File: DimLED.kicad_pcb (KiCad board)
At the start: 2 copper layers, 116 x 26 mm, 15 parts, among them J1 Input Power Terminal, J2 DC005, J3 Conn_01x05, J4 Output LED Terminal, J5 Conn_01x03, SW1 IO BTN, SW2 RST BTN, U1 MP1584 Module, U2 ESP-01, U3 XY-MOS Module

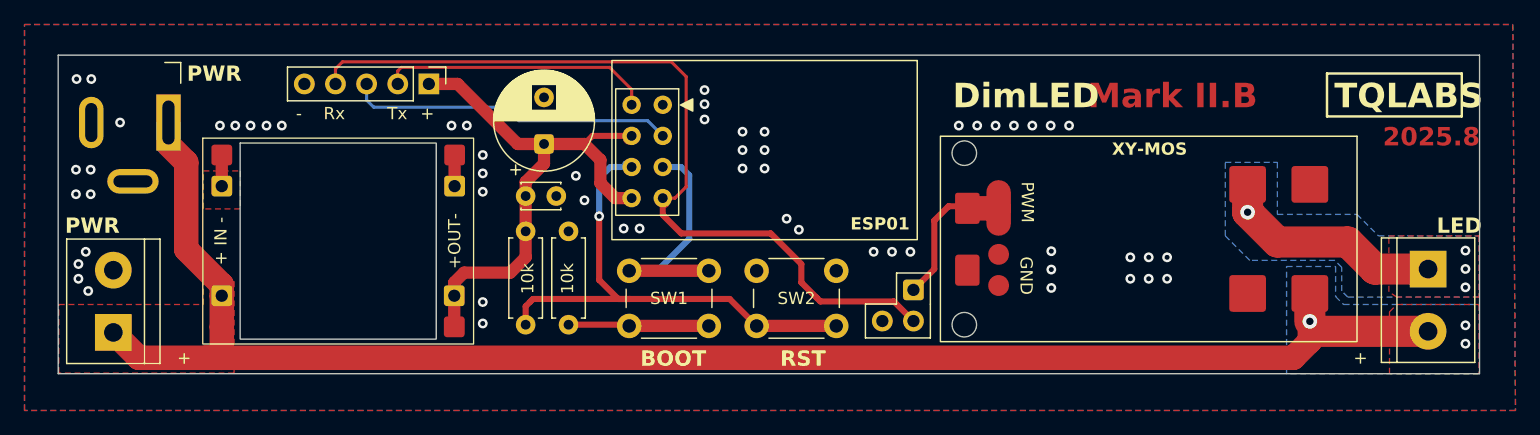
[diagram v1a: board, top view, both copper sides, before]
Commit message: feat: bottom 12v path
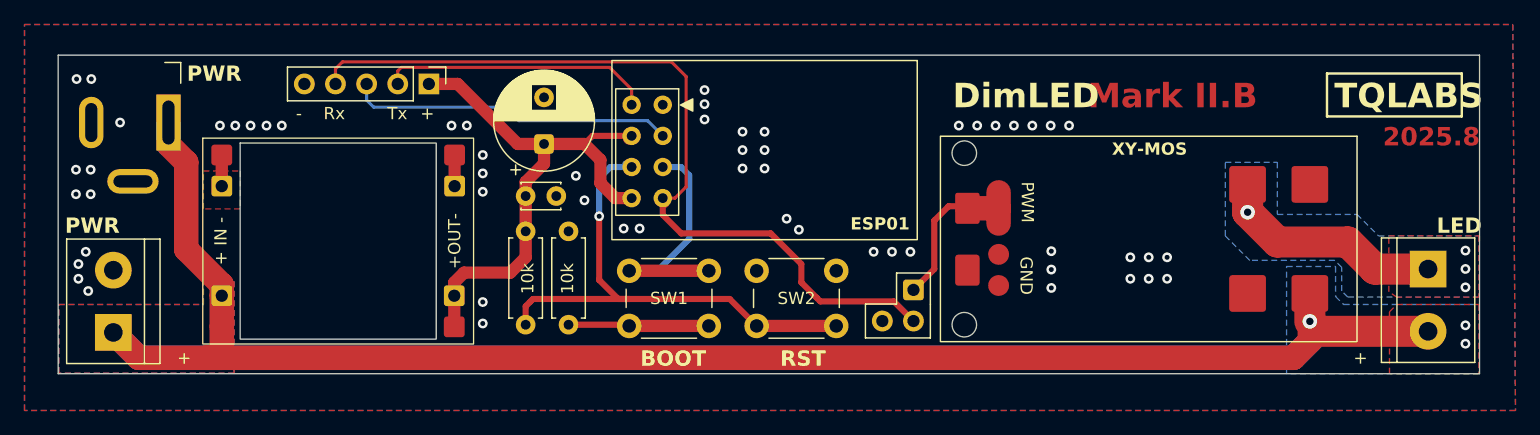
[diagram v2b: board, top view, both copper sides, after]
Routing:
- net +12V: track 134.2 -> 243.2 mm
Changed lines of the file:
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@@
+	)
+	(segment
+		(start 90.319 111.949)
+		(end 184.561475 111.949)
+		(width 2)
+		(layer "B.Cu")
+		(net 5)
 	)
 	(segment
 		(start 92.75 92.75)
 		(end 92.75 94.55)
+		(width 2)
+		(layer "B.Cu")
+		(net 5)
+	)
+	(segment
+		(start 88.25 109.88)
+		(end 90.319 111.949)
+		(width 2)
+		(layer "B.Cu")
+		(net 5)
+	)
+	(segment
+		(start 186.720475 109.79)
+		(end 184.561475 111.949)
+		(width 2)
+		(layer "B.Cu")
+		(net 5)
+	)
+	(segment
+		(start 195.55 109.79)
+		(end 186.720475 109.79)
 		(width 2)
 		(layer "B.Cu")
@@
 	)
 	(zone
-		(net 5)
-		(net_name "+12V")
-		(layer "F.Cu")
-		(hatch edge 0.5)
-		(priority 2)
-		(connect_pads yes
-			(clearance 0.5)
-		)
-		(min_thickness 0.25)
-		(filled_areas_thickness no)
-		(fill yes
-			(thermal_gap 0.5)
-			(thermal_bridge_width 0.5)
-		)
-		(polygon
-			(pts
-				(xy 83.8 107.6) (xy 95.6 107.6) (xy 95.6 105.875) (xy 95.775 105.7) (xy 98.1 105.7) (xy 98.1 113.2)
-				(xy 83.8 113.2)
-			)
-		)
-	)
-	(zone
 		(net 0)
 		(net_name "")
@@
 			)
 		)
+	)
+	(zone
+		(net 5)
+		(net_name "+12V")
+		(layers "F.Cu" "B.Cu")
+		(hatch edge 0.5)
+		(priority 2)
+		(connect_pads yes
+			(clearance 0.5)
+		)
+		(min_thickness 0.25)
+		(filled_areas_thickness no)
+		(fill yes
+			(thermal_gap 0.5)
+			(thermal_bridge_width 0.5)
+		)
+		(polygon
+			(pts
+				(xy 83.8 107.6) (xy 95.6 107.6) (xy 95.6 105.875) (xy 95.775 105.7) (xy 98.1 105.7) (xy 98.1 113.2)
+				(xy 83.8 113.2)
+			)
+		)
